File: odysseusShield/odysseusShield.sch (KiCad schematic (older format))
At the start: 6 parts, among them J1 Conn_01x32, J2 Conn_01x07, Q1 SSM3K333R, Q2 SSM3K333R

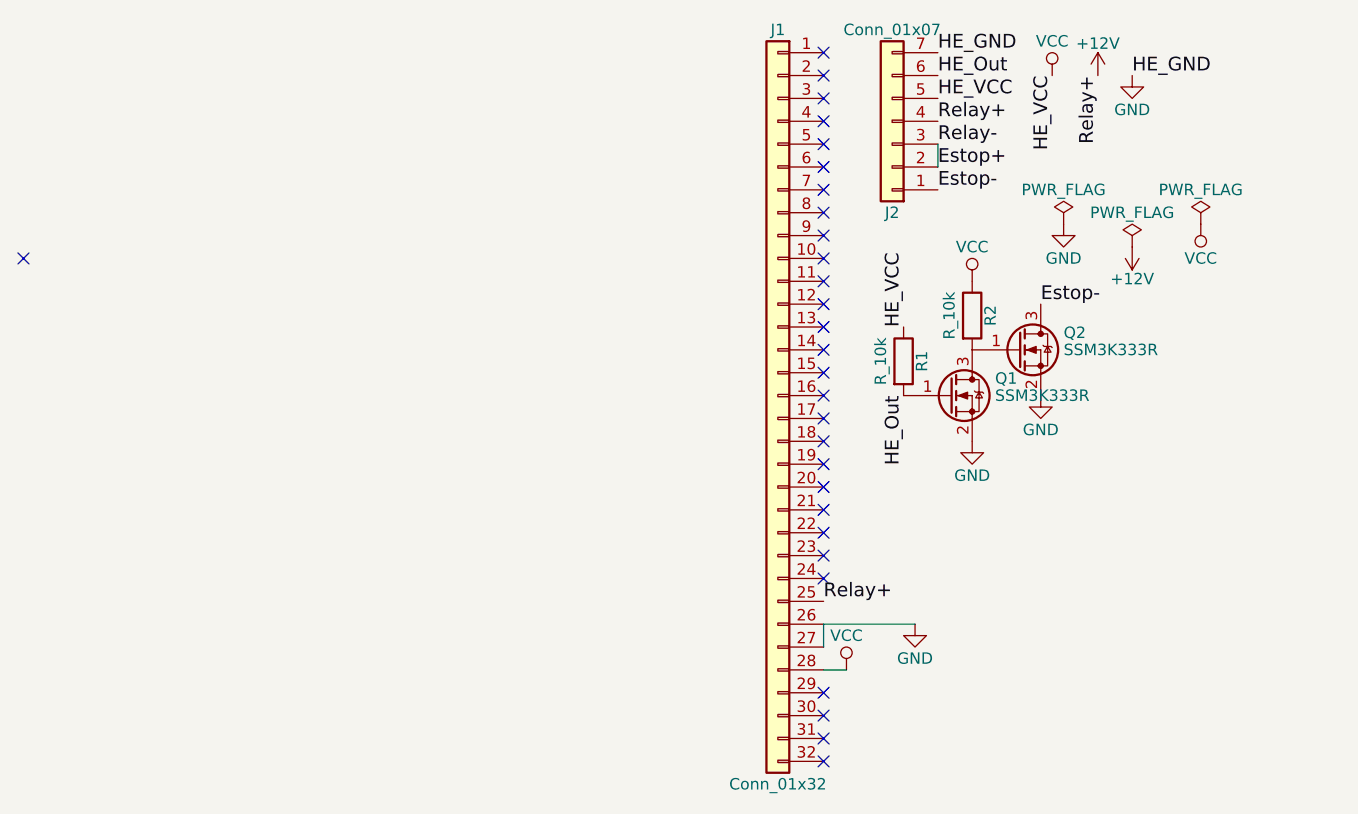
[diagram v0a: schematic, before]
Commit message: working on adding logo to PCB, edited PCB based on joystick and fan additions
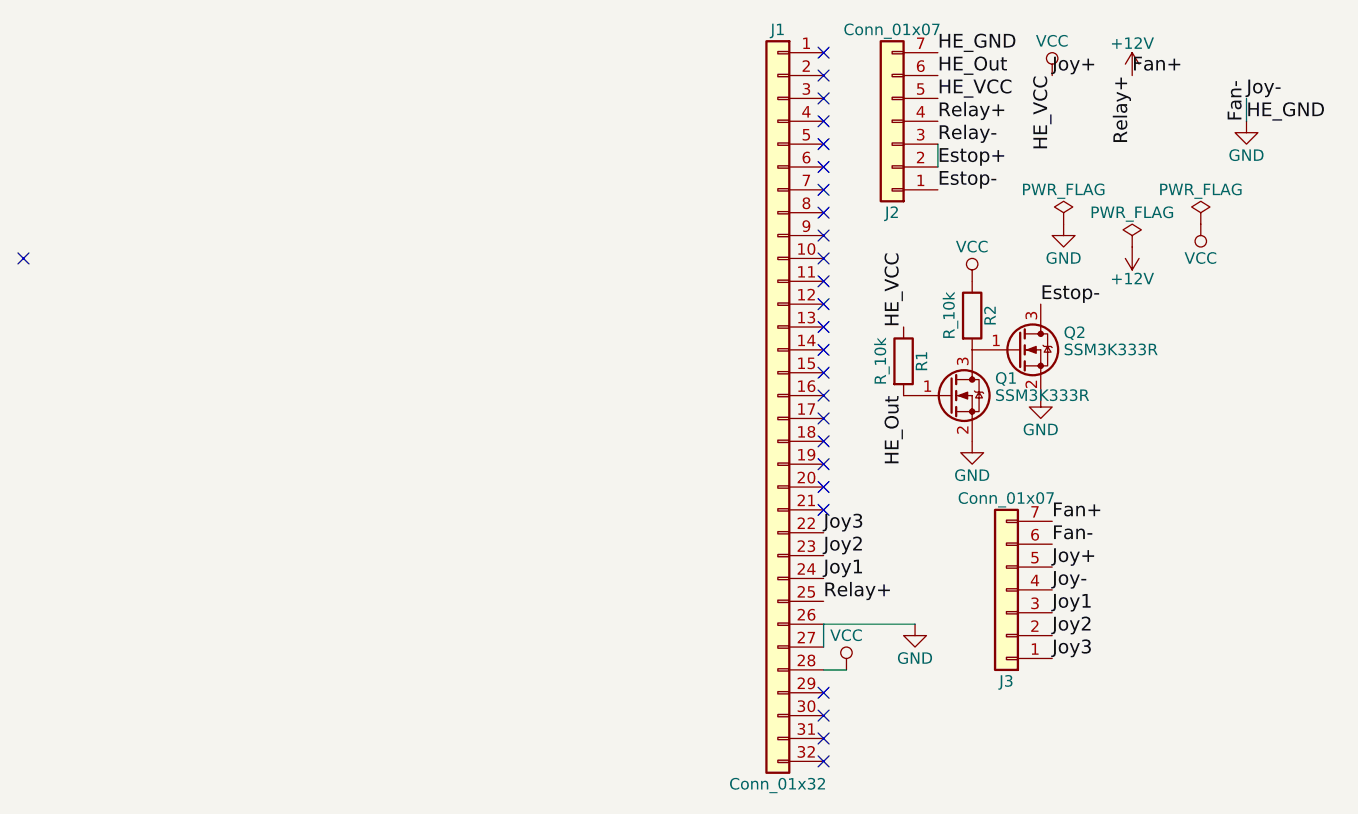
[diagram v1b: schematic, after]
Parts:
- added J3: Conn_01x07, odysseusWindows:Header_P2.54mm_7, symbol Conn_01x07
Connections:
- net +12V: now also J3.7 (Pin_7)
- net GND: now also J3.4 (Pin_4), J3.6 (Pin_6)
- net VCC: now also J3.5 (Pin_5)
- net Joy3: now reaches J1.22 (Pin_22)
- net Joy3: now also J3.1 (Pin_1)
- net Joy2: now reaches J1.23 (Pin_23)
- net Joy2: now also J3.2 (Pin_2)
- net Joy1: now reaches J1.24 (Pin_24)
- net Joy1: now also J3.3 (Pin_3)
- no-connect marks 29 -> 26
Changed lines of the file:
@@
 LIBS:contrib
 LIBS:valves
-LIBS:formula
+LIBS:odysseusShield-cache
 EELAYER 25 0
 EELAYER END
@@
 L GND #PWR03
 U 1 1 5A064617
+P 3350 1950
+F 0 "#PWR03" H 3350 1700 50  0001 C CNN
+F 1 "GND" H 3350 1800 50  0000 C CNN
+F 2 "" H 3350 1950 50  0001 C CNN
+F 3 "" H 3350 1950 50  0001 C CNN
+	1    3350 1950
+	1    0    0    -1
+$EndComp
+$Comp
+L +12V #PWR04
+U 1 1 5A064633
 P 2850 1750
-F 0 "#PWR03" H 2850 1500 50  0001 C CNN
-F 1 "GND" H 2850 1600 50  0000 C CNN
+F 0 "#PWR04" H 2850 1600 50  0001 C CNN
+F 1 "+12V" H 2850 1890 50  0000 C CNN
 F 2 "" H 2850 1750 50  0001 C CNN
 F 3 "" H 2850 1750 50  0001 C CNN
@@
 	1    0    0    -1
 $EndComp
-$Comp
-L +12V #PWR04
-U 1 1 5A064633
-P 2700 1750
-F 0 "#PWR04" H 2700 1600 50  0001 C CNN
-F 1 "+12V" H 2700 1890 50  0000 C CNN
-F 2 "" H 2700 1750 50  0001 C CNN
-F 3 "" H 2700 1750 50  0001 C CNN
-	1    2700 1750
-	1    0    0    -1
-$EndComp
-Text Label 2700 1750 3    60   ~ 0
+Text Label 2850 1750 3    60   ~ 0
 Relay+
-Text Label 2850 1750 0    60   ~ 0
+Text Label 3350 1950 0    60   ~ 0
 HE_GND
 Text Label 2500 1750 3    60   ~ 0
@@
 NoConn ~ 1500 4550
 NoConn ~ 1500 4450
-NoConn ~ 1500 3950
-NoConn ~ 1500 3850
-NoConn ~ 1500 3750
 NoConn ~ 1500 3650
 NoConn ~ 1500 3550
@@
 NoConn ~ 1500 1650
 NoConn ~ -2000 2550
+$Comp
+L Conn_01x07 J3
+U 1 1 5A0F7574
+P 2300 4000
+F 0 "J3" H 2300 4400 50  0000 C CNN
+F 1 "Conn_01x07" H 2300 3600 50  0000 C CNN
+F 2 "odysseusWindows:Header_P2.54mm_7" H 2300 4000 50  0001 C CNN
+F 3 "" H 2300 4000 50  0001 C CNN
+	1    2300 4000
+	-1   0    0    1
+$EndComp
+Text Label 2500 3700 0    60   ~ 0
+Fan+
+Text Label 2500 3800 0    60   ~ 0
+Fan-
+Text Label 2500 3900 0    60   ~ 0
+Joy+
+Text Label 2500 4000 0    60   ~ 0
+Joy-
+Text Label 2500 4100 0    60   ~ 0
+Joy1
+Text Label 2500 4200 0    60   ~ 0
+Joy2
+Text Label 2500 4300 0    60   ~ 0
+Joy3
+Text Label 2850 1750 0    60   ~ 0
+Fan+
+Text Label 3350 1950 1    60   ~ 0
+Fan-
+Text Label 3350 1850 0    60   ~ 0
+Joy-
+Wire Wire Line
+	3350 1950 3350 1850
+Text Label 2500 1750 0    60   ~ 0
+Joy+
+Text Label 1500 3750 0    60   ~ 0
+Joy3
+Text Label 1500 3850 0    60   ~ 0
+Joy2
+Text Label 1500 3950 0    60   ~ 0
+Joy1
 $EndSCHEMATC

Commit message: added labels to pins and indicator leds
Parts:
- added D1, D2: LED_0805, footprints:LED_0805_OEM, symbol LED_0805
- added R3: R_200, footprints:R_0805_OEM, symbol R_200
- added R4: R_1k, footprints:R_0805_OEM, symbol R_1k
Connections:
- net +12V: now also R4.1
- net GND: now also D1.1 (K), D2.1 (K)
- net VCC: now also R3.1
- new net: D1.2 (A), R3.2
- new net: D2.2 (A), R4.2
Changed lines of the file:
@@
 LIBS:contrib
 LIBS:valves
+LIBS:formula
 LIBS:odysseusShield-cache
 EELAYER 25 0
@@
 Text Label 1500 3950 0    60   ~ 0
 Joy1
+$Comp
+L LED_0805 D1
+U 1 1 5A11F581
+P 3265 3450
+F 0 "D1" H 3265 3350 50  0000 C CNN
+F 1 "LED_0805" H 3265 3550 50  0000 C CNN
+F 2 "footprints:LED_0805_OEM" H 3165 3450 50  0001 C CNN
+F 3 "http://www.osram-os.com/Graphics/XPic9/00078860_0.pdf" H 3265 3550 50  0001 C CNN
+F 4 "475-1410-1-ND" H 3265 3450 60  0001 C CNN "MPN"
+F 5 "Digi-Key" H 3265 3450 60  0001 C CNN "MFN"
+F 6 "Value" H 3265 3450 60  0001 C CNN "Package"
+F 7 "https://www.digikey.com/products/en?keywords=475-1410-1-ND" H 3665 3950 60  0001 C CNN "PurchasingLink"
+	1    3265 3450
+	0    -1   -1   0
+$EndComp
+$Comp
+L LED_0805 D2
+U 1 1 5A11F61C
+P 3545 3450
+F 0 "D2" H 3545 3350 50  0000 C CNN
+F 1 "LED_0805" H 3545 3550 50  0000 C CNN
+F 2 "footprints:LED_0805_OEM" H 3445 3450 50  0001 C CNN
+F 3 "http://www.osram-os.com/Graphics/XPic9/00078860_0.pdf" H 3545 3550 50  0001 C CNN
+F 4 "475-1410-1-ND" H 3545 3450 60  0001 C CNN "MPN"
+F 5 "Digi-Key" H 3545 3450 60  0001 C CNN "MFN"
+F 6 "Value" H 3545 3450 60  0001 C CNN "Package"
+F 7 "https://www.digikey.com/products/en?keywords=475-1410-1-ND" H 3945 3950 60  0001 C CNN "PurchasingLink"
+	1    3545 3450
+	0    -1   -1   0
+$EndComp
+$Comp
+L R_200 R3
+U 1 1 5A11F67F
+P 3265 3150
+F 0 "R3" V 3345 3150 50  0000 C CNN
+F 1 "R_200" V 3165 3150 50  0000 C CNN
+F 2 "footprints:R_0805_OEM" H 3195 3150 50  0001 C CNN
+F 3 "https://www.seielect.com/Catalog/SEI-RMCF_RMCP.pdf" H 3345 3150 50  0001 C CNN
+F 4 "Digi-Key" H 3265 3150 60  0001 C CNN "MFN"
+F 5 "RMCF0805JT200RCT-ND" H 3265 3150 60  0001 C CNN "MPN"
+F 6 "Value" H 3265 3150 60  0001 C CNN "Package"
+F 7 "https://www.digikey.com/products/en?keywords=RMCF0805JT200RCT-ND" H 3745 3550 60  0001 C CNN "PurchasingLink"
+	1    3265 3150
+	1    0    0    -1
+$EndComp
+$Comp
+L +12V #PWR015
+U 1 1 5A11F88C
+P 3545 3000
+F 0 "#PWR015" H 3545 2850 50  0001 C CNN
+F 1 "+12V" H 3545 3140 50  0000 C CNN
+F 2 "" H 3545 3000 50  0001 C CNN
+F 3 "" H 3545 3000 50  0001 C CNN
+	1    3545 3000
+	1    0    0    -1
+$EndComp
+$Comp
+L R_1k R4
+U 1 1 5A11F938
+P 3545 3150
+F 0 "R4" V 3625 3150 50  0000 C CNN
+F 1 "R_1k" V 3445 3150 50  0000 C CNN
+F 2 "footprints:R_0805_OEM" H 3475 3150 50  0001 C CNN
+F 3 "https://www.seielect.com/Catalog/SEI-rncp.pdf" H 3625 3150 50  0001 C CNN
+F 4 "Digi-Key" H 3545 3150 60  0001 C CNN "MFN"
+F 5 "RNCP0805FTD1K00CT-ND" H 3545 3150 60  0001 C CNN "MPN"
+F 6 "Value" H 3545 3150 60  0001 C CNN "Package"
+F 7 "https://www.digikey.com/products/en?keywords=RNCP0805FTD1K00CT-ND" H 4025 3550 60  0001 C CNN "PurchasingLink"
+	1    3545 3150
+	1    0    0    -1
+$EndComp
+$Comp
+L VCC #PWR016
+U 1 1 5A11F995
+P 3265 3000
+F 0 "#PWR016" H 3265 2850 50  0001 C CNN
+F 1 "VCC" H 3265 3150 50  0000 C CNN
+F 2 "" H 3265 3000 50  0001 C CNN
+F 3 "" H 3265 3000 50  0001 C CNN
+	1    3265 3000
+	1    0    0    -1
+$EndComp
+$Comp
+L GND #PWR017
+U 1 1 5A11F9BF
+P 3265 3600
+F 0 "#PWR017" H 3265 3350 50  0001 C CNN
+F 1 "GND" H 3265 3450 50  0000 C CNN
+F 2 "" H 3265 3600 50  0001 C CNN
+F 3 "" H 3265 3600 50  0001 C CNN
+	1    3265 3600
+	1    0    0    -1
+$EndComp
+$Comp
+L GND #PWR018
+U 1 1 5A11F9E9
+P 3545 3600
+F 0 "#PWR018" H 3545 3350 50  0001 C CNN
+F 1 "GND" H 3545 3450 50  0000 C CNN
+F 2 "" H 3545 3600 50  0001 C CNN
+F 3 "" H 3545 3600 50  0001 C CNN
+	1    3545 3600
+	1    0    0    -1
+$EndComp
 $EndSCHEMATC
